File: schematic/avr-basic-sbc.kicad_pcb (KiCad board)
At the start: 2 copper layers, 94 x 55 mm, 38 parts, among them J1 DC-005 Power Jack, J2 PS/2 keyboard port, J3 RCA Video Jack, J4 Port B, J5 Port A, J6 Port C, J7 Port D, J8 USBasp header, J9 Power output header, U1 ATmega1284P-P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

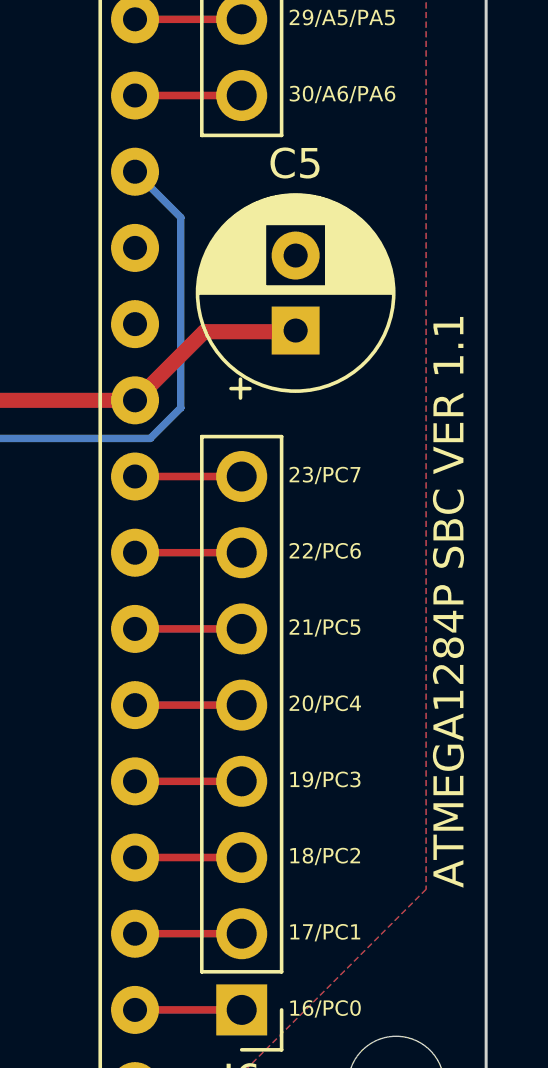
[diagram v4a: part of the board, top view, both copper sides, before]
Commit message: AVR-SBC board updated: Silkscreen version number updated
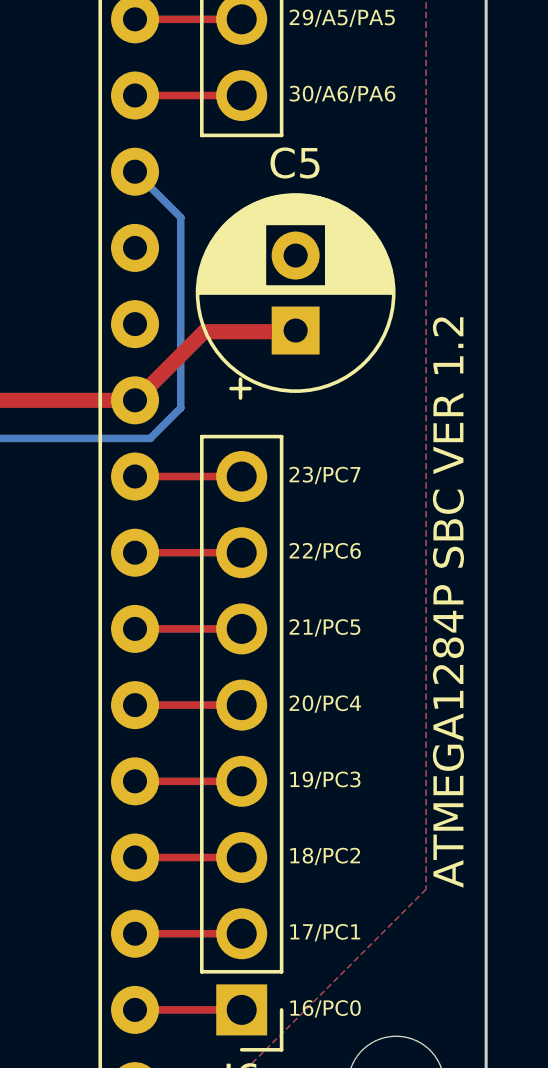
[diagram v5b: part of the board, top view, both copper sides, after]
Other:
- board text added: "ATMEGA1284P SBC VER 1.2"
- board text removed: "ATMEGA1284P SBC VER 1.1"
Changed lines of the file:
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@@
     (effects (font (size 1 1) (thickness 0.15)) (justify left bottom))
   )
-  (gr_text "ATMEGA1284P SBC VER 1.1" (at 93.365 44.958 90) (layer "F.SilkS")
+  (gr_text "ATMEGA1284P SBC VER 1.2" (at 93.365 44.958 90) (layer "F.SilkS")
     (effects (font (size 1 1) (thickness 0.15)) (justify left bottom))
   )

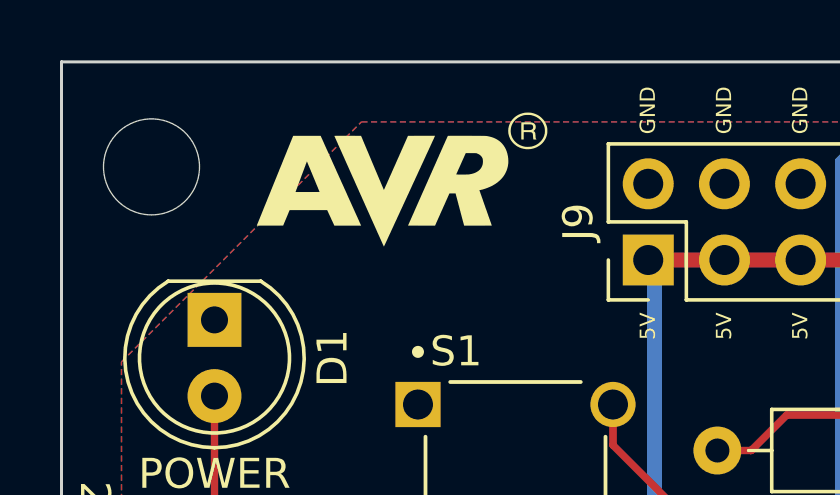
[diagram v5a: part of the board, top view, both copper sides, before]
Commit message: AVR-SBC board updated: Silkscreen updated
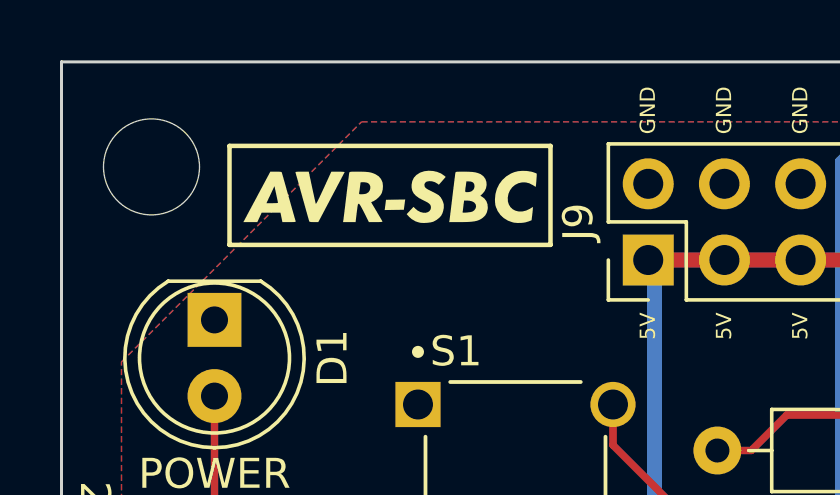
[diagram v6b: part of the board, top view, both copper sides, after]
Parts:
- moved GRAPHICS1 0.48 mm to (11.0, 4.50)

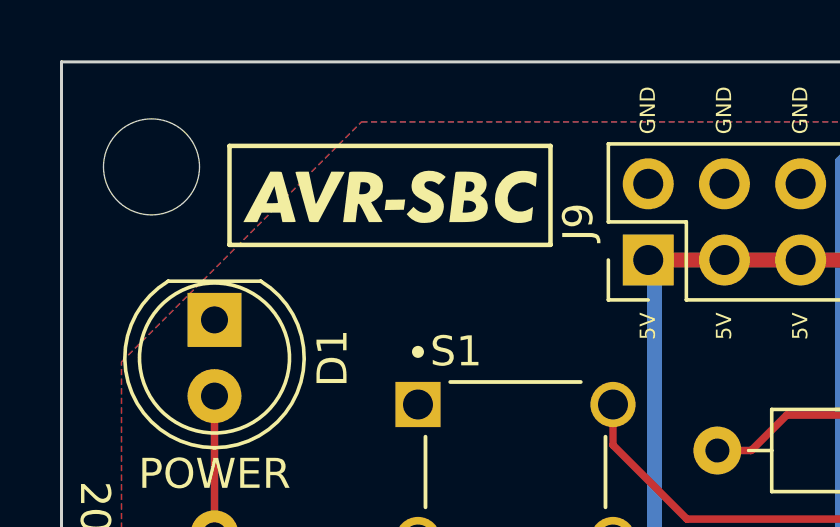
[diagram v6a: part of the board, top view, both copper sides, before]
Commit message: AVR-SBC board updated: Silkscreen updated
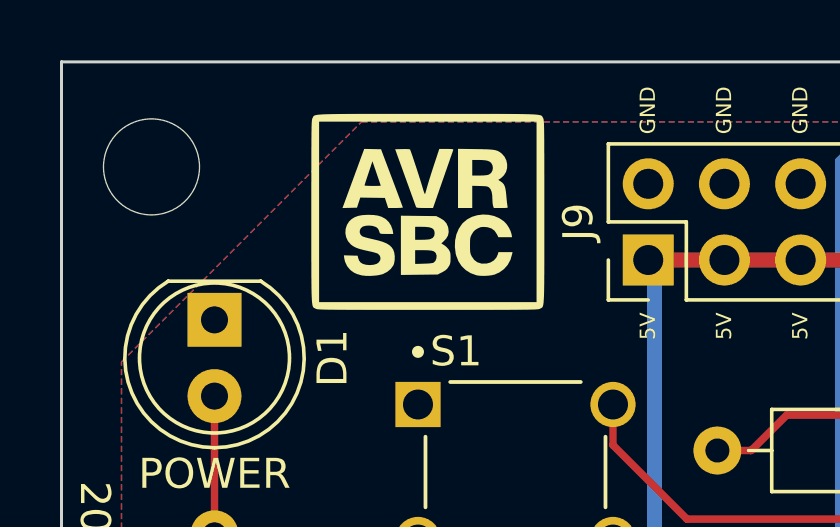
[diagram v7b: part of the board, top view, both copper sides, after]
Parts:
- removed GRAPHICS1: LOGO, LOGO
- added G2: LOGO, LOGO, F.Cu at (12.2, 5.00)
